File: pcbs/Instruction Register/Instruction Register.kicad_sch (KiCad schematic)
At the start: 7 parts, among them J1001 Conn_02x20_Odd_Even, J1002 Conn_02x20_Odd_Even, U1001 74HC245, U1002 74HC245, U1003 74HC245, U1004 74HC245

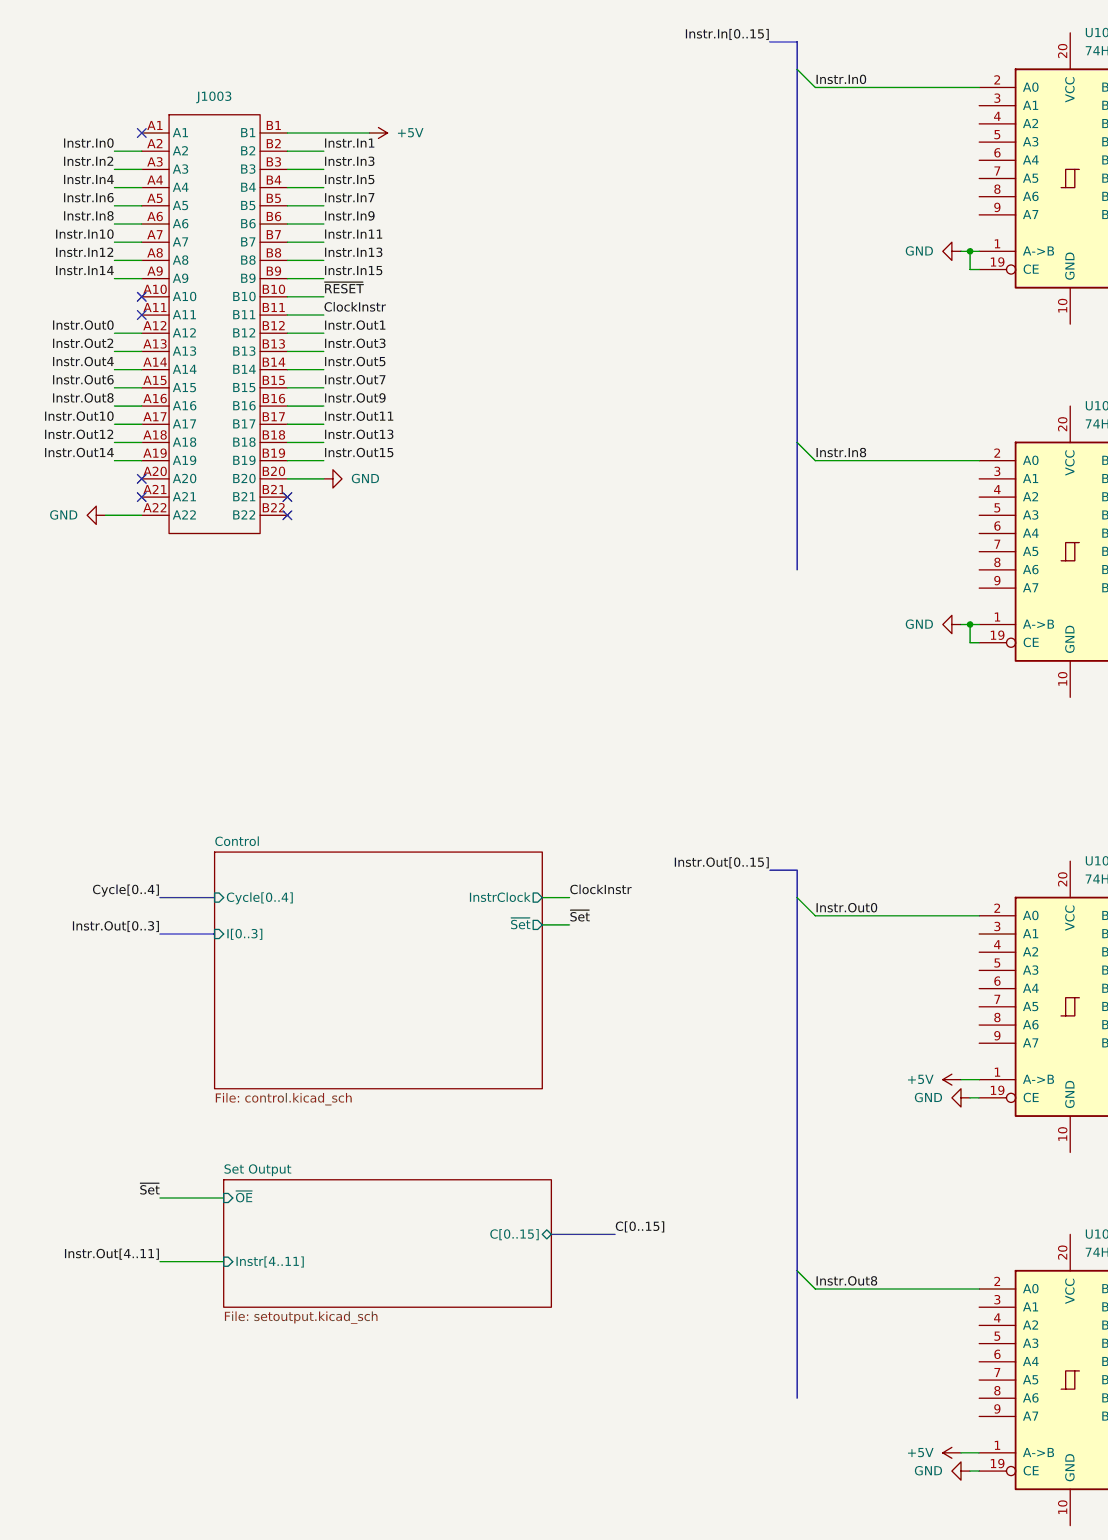
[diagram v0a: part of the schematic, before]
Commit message: Tweaking schematic and basic routing
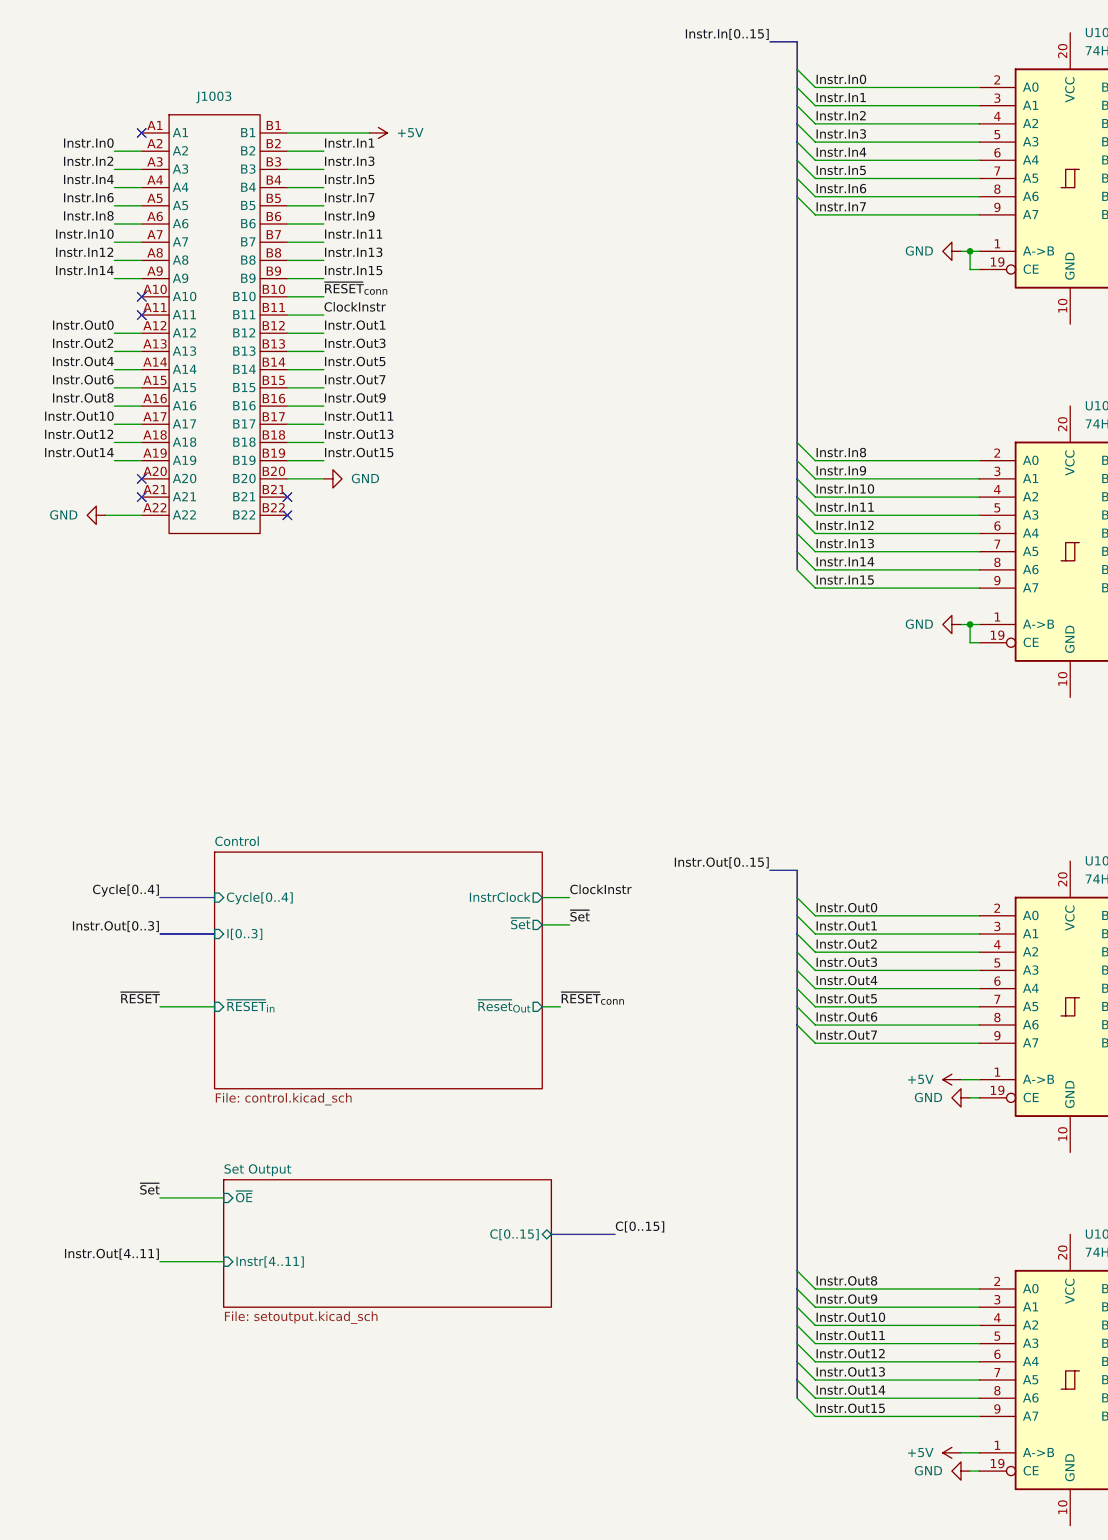
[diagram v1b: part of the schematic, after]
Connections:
- net Instr.In1: now also U1001.3 (A1)
- net Instr.In10: now also U1002.4 (A2)
- net Instr.In11: now also U1002.5 (A3)
- net Instr.In12: now also U1002.6 (A4)
- net Instr.In13: now also U1002.7 (A5)
- net Instr.In14: now also U1002.8 (A6)
- net Instr.In15: now also U1002.9 (A7)
- net Instr.In2: now also U1001.4 (A2)
- net Instr.In3: now also U1001.5 (A3)
- net Instr.In4: now also U1001.6 (A4)
- net Instr.In5: now also U1001.7 (A5)
- net Instr.In6: now also U1001.8 (A6)
- net Instr.In7: now also U1001.9 (A7)
- net Instr.In9: now also U1002.3 (A1)
- net Instr.Out1: now also U1003.3 (A1)
- net Instr.Out10: now also U1004.4 (A2)
- net Instr.Out11: now also U1004.5 (A3)
- net Instr.Out12: now also U1004.6 (A4)
- net Instr.Out13: now also U1004.7 (A5)
- net Instr.Out14: now also U1004.8 (A6)
- net Instr.Out15: now also U1004.9 (A7)
- net Instr.Out2: now also U1003.4 (A2)
- net Instr.Out3: now also U1003.5 (A3)
- net Instr.Out4: now also U1003.6 (A4)
- net Instr.Out5: now also U1003.7 (A5)
- net Instr.Out6: now also U1003.8 (A6)
- net Instr.Out7: now also U1003.9 (A7)
- net Instr.Out9: now also U1004.3 (A1)
- net ~{RESET}: no longer J1003.B10
- new net ~{RESET}_{conn}: J1003.B10
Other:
- sheet Control ports: added ~{RESET}_{in}, ~{Reset}_{Out}; removed none

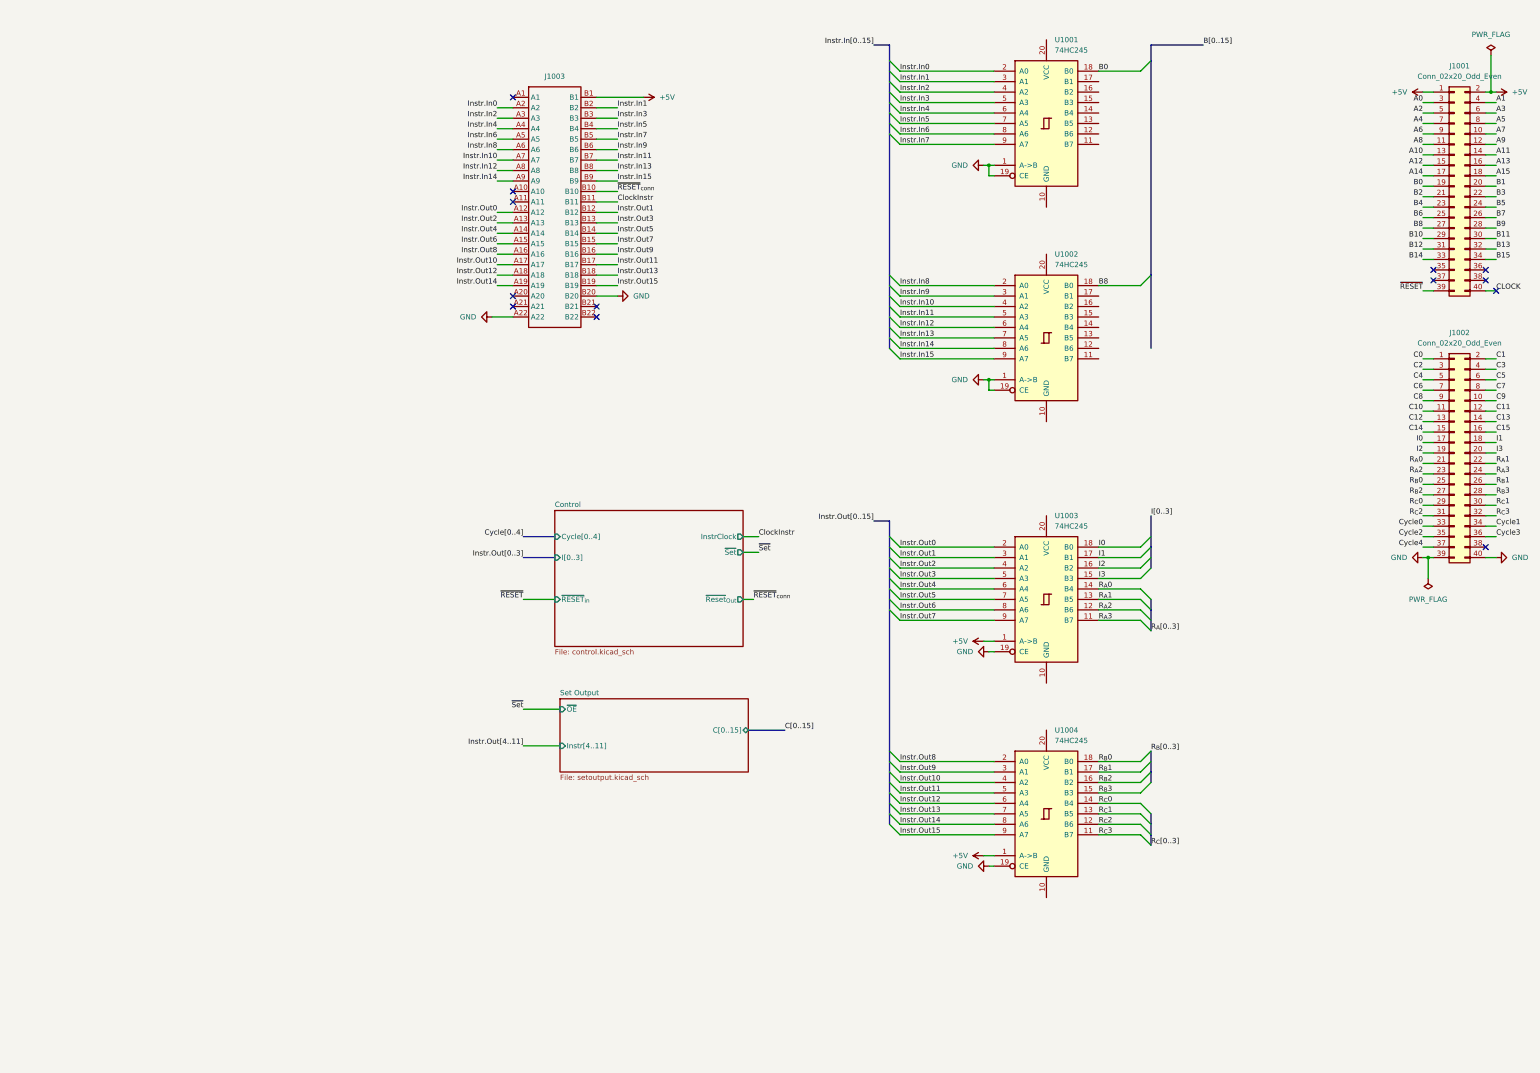
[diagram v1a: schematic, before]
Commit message: Completing routing; needs silkscreen
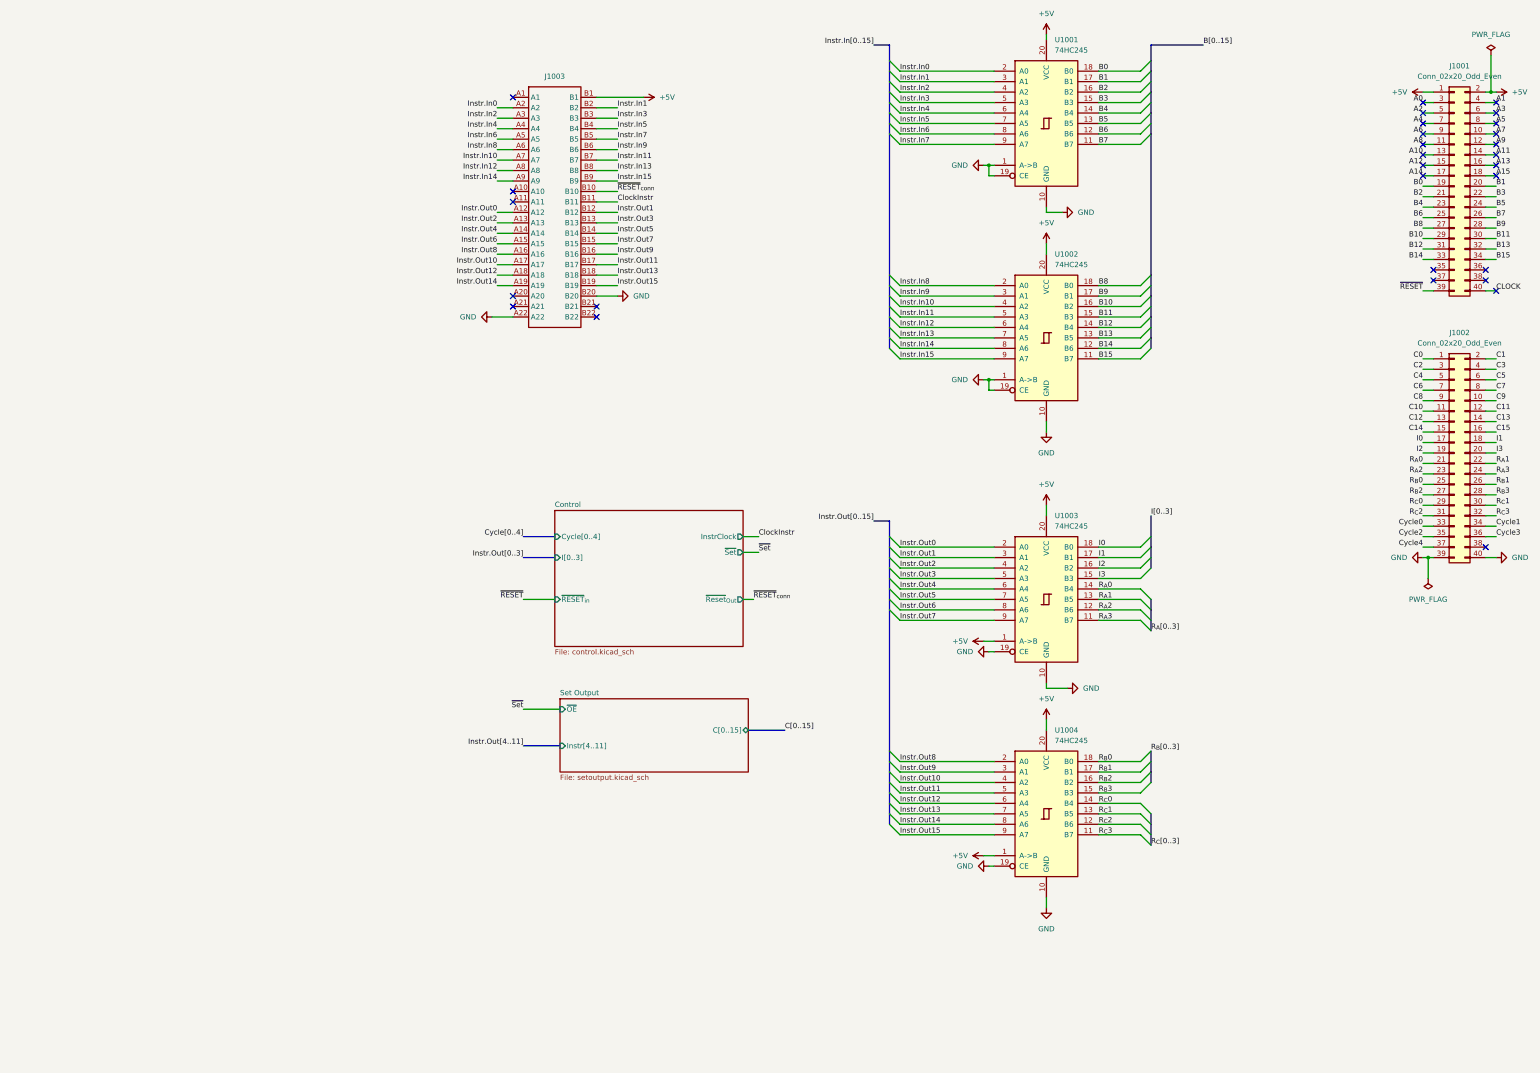
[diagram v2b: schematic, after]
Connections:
- net +5V: now also U1001.20 (VCC), U1002.20 (VCC), U1003.20 (VCC), U1004.20 (VCC)
- net B1: now also U1001.17 (B1)
- net B10: now also U1002.16 (B2)
- net B11: now also U1002.15 (B3)
- net B12: now also U1002.14 (B4)
- net B13: now also U1002.13 (B5)
- net B14: now also U1002.12 (B6)
- net B15: now also U1002.11 (B7)
- net B2: now also U1001.16 (B2)
- net B3: now also U1001.15 (B3)
- net B4: now also U1001.14 (B4)
- net B5: now also U1001.13 (B5)
- net B6: now also U1001.12 (B6)
- net B7: now also U1001.11 (B7)
- net B9: now also U1002.17 (B1)
- net GND: now also U1001.10 (GND), U1002.10 (GND), U1003.10 (GND), U1004.10 (GND)
- no-connect marks 13 -> 29

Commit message: Preliminary final layout
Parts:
- added H1001, H1002, H1003, H1004: MountingHole, MountingHole:MountingHole_2.7mm_M2.5_ISO7380, symbol Mechanical:MountingHole
